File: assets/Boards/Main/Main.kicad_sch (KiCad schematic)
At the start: 15 parts, among them J1 PWR, J2 CTRLS_BOARD, U1 DFRobot_MAX98357, U2 Waveshare_ESP32-S3-Tiny

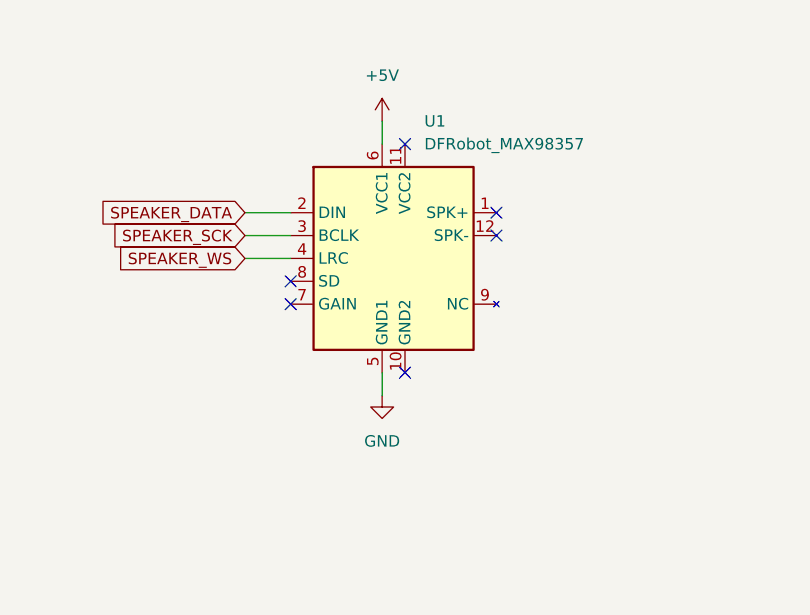
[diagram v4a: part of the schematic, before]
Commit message: Applied suggestions from people from the KiCad forum.
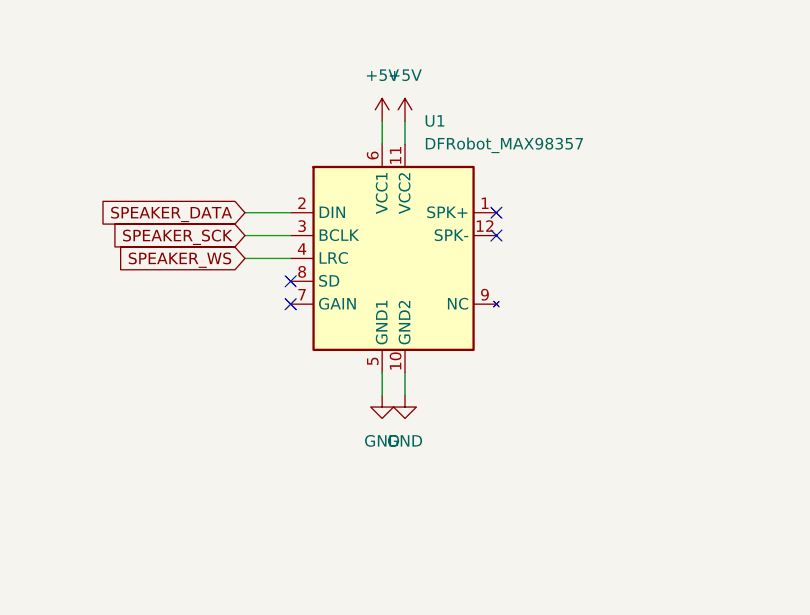
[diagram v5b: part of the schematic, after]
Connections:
- net +5V: now also U1.11 (VCC2)
- net GND: now also U1.10 (GND2)
- no-connect marks 18 -> 16
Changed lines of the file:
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@@
-	)
-	(no_connect
-		(at 134.62 34.29)
 	)
 	(no_connect
@@
 	)
 	(no_connect
-		(at 134.62 59.69)
-	)
-	(no_connect
 		(at 144.78 44.45)
 	)
@@
 	(wire
 		(pts
+			(xy 134.62 59.69) (xy 134.62 62.23)
+		)
+		(stroke
+			(width 0)
+			(type default)
+		)
+	)
+	(wire
+		(pts
 			(xy 132.08 31.75) (xy 132.08 34.29)
 		)
@@
 		(pts
 			(xy 158.75 121.92) (xy 144.78 121.92)
+		)
+		(stroke
+			(width 0)
+			(type default)
+		)
+	)
+	(wire
+		(pts
+			(xy 134.62 31.75) (xy 134.62 34.29)
 		)
 		(stroke
@@
 	)
 	(symbol
+		(lib_id "power:+5V")
+		(at 134.62 31.75 0)
+		(unit 1)
+		(exclude_from_sim no)
+		(in_bom yes)
+		(on_board yes)
+		(dnp no)
+		(fields_autoplaced yes)
+		(property "Reference" "#PWR010"
+			(at 134.62 35.56 0)
+			(effects
+				(font
+					(size 1.27 1.27)
+				)
+				(hide yes)
+			)
+		)
+		(property "Value" "+5V"
+			(at 134.62 26.67 0)
+			(effects
+				(font
+					(size 1.27 1.27)
+				)
+			)
+		)
+		(property "Footprint" ""
+			(at 134.62 31.75 0)
+			(effects
+				(font
+					(size 1.27 1.27)
+				)
+				(hide yes)
+			)
+		)
+		(property "Datasheet" ""
+			(at 134.62 31.75 0)
+			(effects
+				(font
+					(size 1.27 1.27)
+				)
+				(hide yes)
+			)
+		)
+		(property "Description" "Power symbol creates a global label with name \"+5V\""
+			(at 134.62 31.75 0)
+			(effects
+				(font
+					(size 1.27 1.27)
+				)
+				(hide yes)
+			)
+		)
+		(pin "1"
+		)
+		(instances
+			(project "Main"
+				(path "/5d161dc1-54ae-4b00-a0d5-234581851ead"
+					(reference "#PWR010")
+					(unit 1)
+				)
+			)
+		)
+	)
+	(symbol
 		(lib_id "Custom Symbols:Solder_pad")
 		(at 53.34 24.13 0)
@@
 					(unit 1)
 				)
+			)
+		)
+	)
+	(symbol
+		(lib_id "power:GND")
+		(at 134.62 62.23 0)
+		(unit 1)
+		(exclude_from_sim no)
+		(in_bom yes)
+		(on_board yes)
+		(dnp no)
+		(fields_autoplaced yes)
+		(property "Reference" "#PWR09"
+			(at 134.62 68.58 0)
+			(effects
+				(font
+					(size 1.27 1.27)
+				)
+				(hide yes)
+			)
+		)
+		(property "Value" "GND"
+			(at 134.62 67.31 0)
+			(effects
+				(font
+					(size 1.27 1.27)
+				)
+			)
+		)
+		(property "Footprint" ""
+			(at 134.62 62.23 0)
+			(effects
+				(font
+					(size 1.27 1.27)
+				)
+				(hide yes)
+			)
+		)
+		(property "Datasheet" ""
+			(at 134.62 62.23 0)
+			(effects
+				(font
+					(size 1.27 1.27)
+				)
+				(hide yes)
+			)
+		)
+		(property "Description" "Power symbol creates a global label with name \"GND\" , ground"
+			(at 134.62 62.23 0)
+			(effects
+				(font
+					(size 1.27 1.27)
+				)
+				(hide yes)
+			)
+		)
+		(pin "1"
+		)
+		(instances
+			(project "Main"
+				(path "/5d161dc1-54ae-4b00-a0d5-234581851ead"
+					(reference "#PWR09")
+					(unit 1)
+				)
